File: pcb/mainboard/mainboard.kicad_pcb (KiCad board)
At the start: 10 copper layers, 585 parts, among them J1 CONN_PCIE_PWR_8PIN, J10 FAN_01, J11 XILINX_JTAG, J12 JUMPER_0402_SPDT, J13 JUMPER_0402_SPDT, J14 RJ45, J15 PMOD_HOST, J16 SMPM, J17 SMPM, J18 SMPM, J19 SMPM, J2 CONN_IBC_MGMT, J20 SMPM, J21 SMPM, J22 SMPM, J23 SMPM, J24 SMPM, J25 SMPM, J26 SMPM, J27 0826-1G1T-23-F, J28 SMPM, J29 SMPM, J3 CONN_01X03, J30 SMPM, J31 SMPM, J32 SMPM, J33 SMPM, J34 SMPM, J35 SMPM, J36 SMPM, J37 SMPM, J38 SMPM, J39 SMPM, J4 CONN_01X05, J40 SMPM, J41 SMPM, J42 SMPM, J43 SMPM, J44 SMPM, J45 SMPM, J46 SMPM, J47 SMPM, J48 CONN_01X10, J5 XILINX_JTAG, J6 CONN_SFP_HOST, J7 SFP_CAGE, J8 FAN_01, J9 CONN_01X03, K1 RELAY_TE_HF3_96, K2 RELAY_TE_HF3_96, K3 RELAY_TE_HF3_96, K4 RELAY_TE_HF3_96, M1 960-23-23-F-AB-0, SW1 SWITCH, SW2 SWITCH, U1 STM32L031C6U6, U10 MAX40026, U11 MAX40026, U12 MAX40026, U13 MAX40026, U14 MAX40026, U15 MAX40026, U16 MAX40026, U17 MAX40026, U18 MAX40026, U19 MAX40026, U2 MYMGK1R812ERSR, U20 MAX40026, U21 DAC60508, U22 DAC60508, U23 STM32H735-UFBGA176-25, U24 AT24MAC402, U25 ADM3101E_QFN, U26 LMR70503, U27 SIT9121AI-2BF-XXS200.000000G, U28 SIT9121AI-2BF-XXS156.250000G, U29 HMC675LP3E, U3 MYMGK00504ERSR, U30 SIT9121AI-2BF-XXS200.000000G, U31 ECS-1612MV-250-CN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

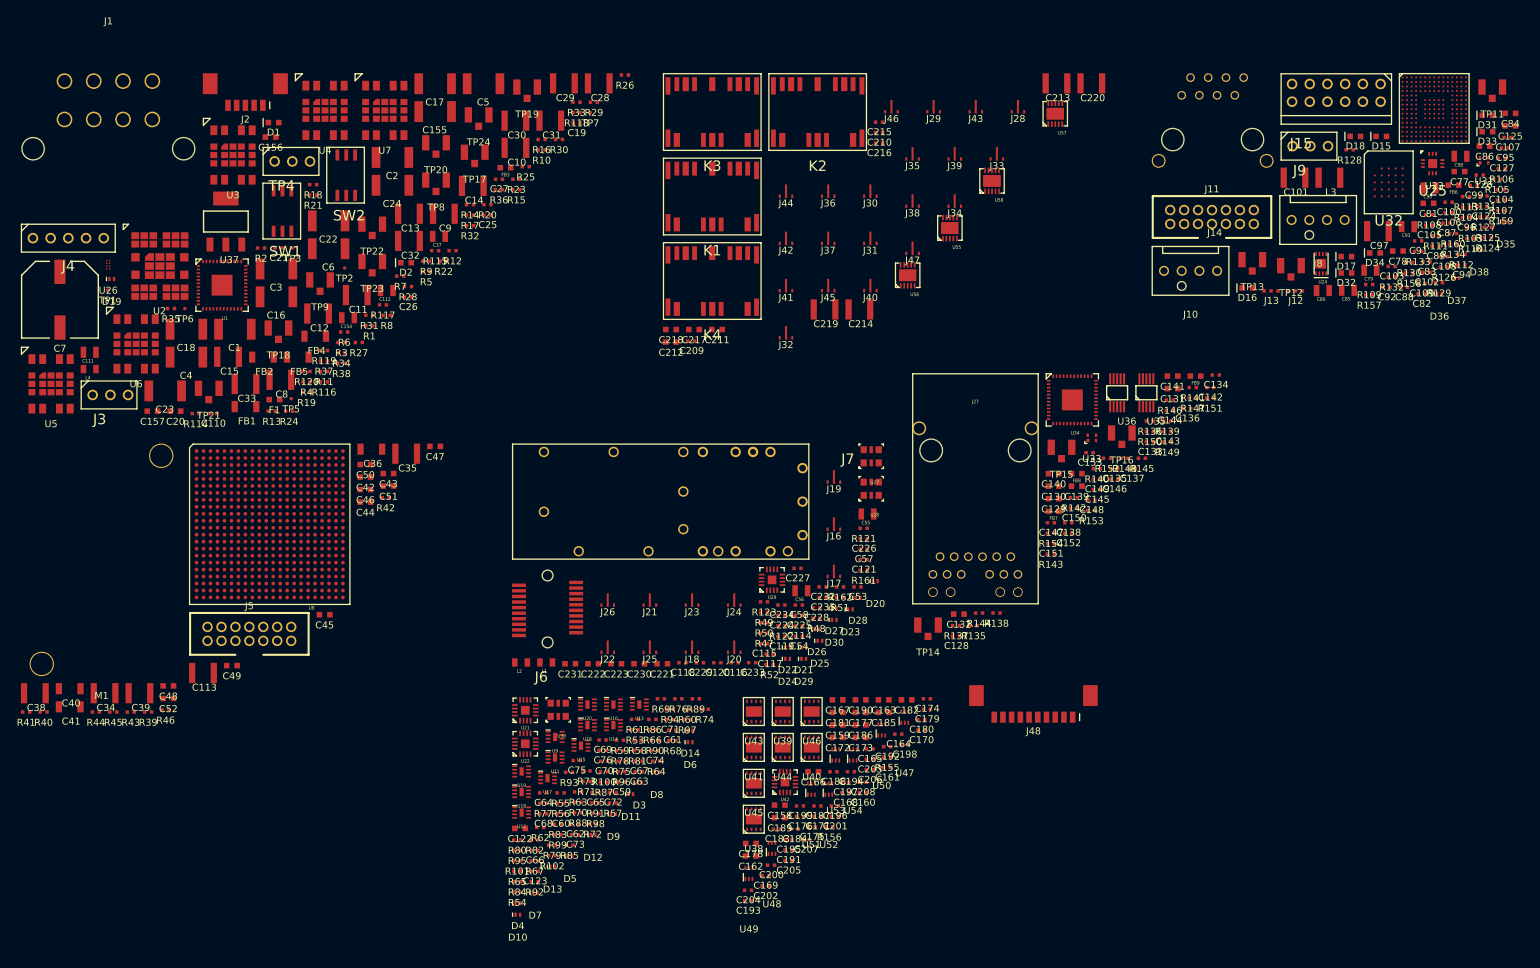
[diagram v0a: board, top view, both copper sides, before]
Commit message: Finished initial schematic review of trigger crossbar mainboard
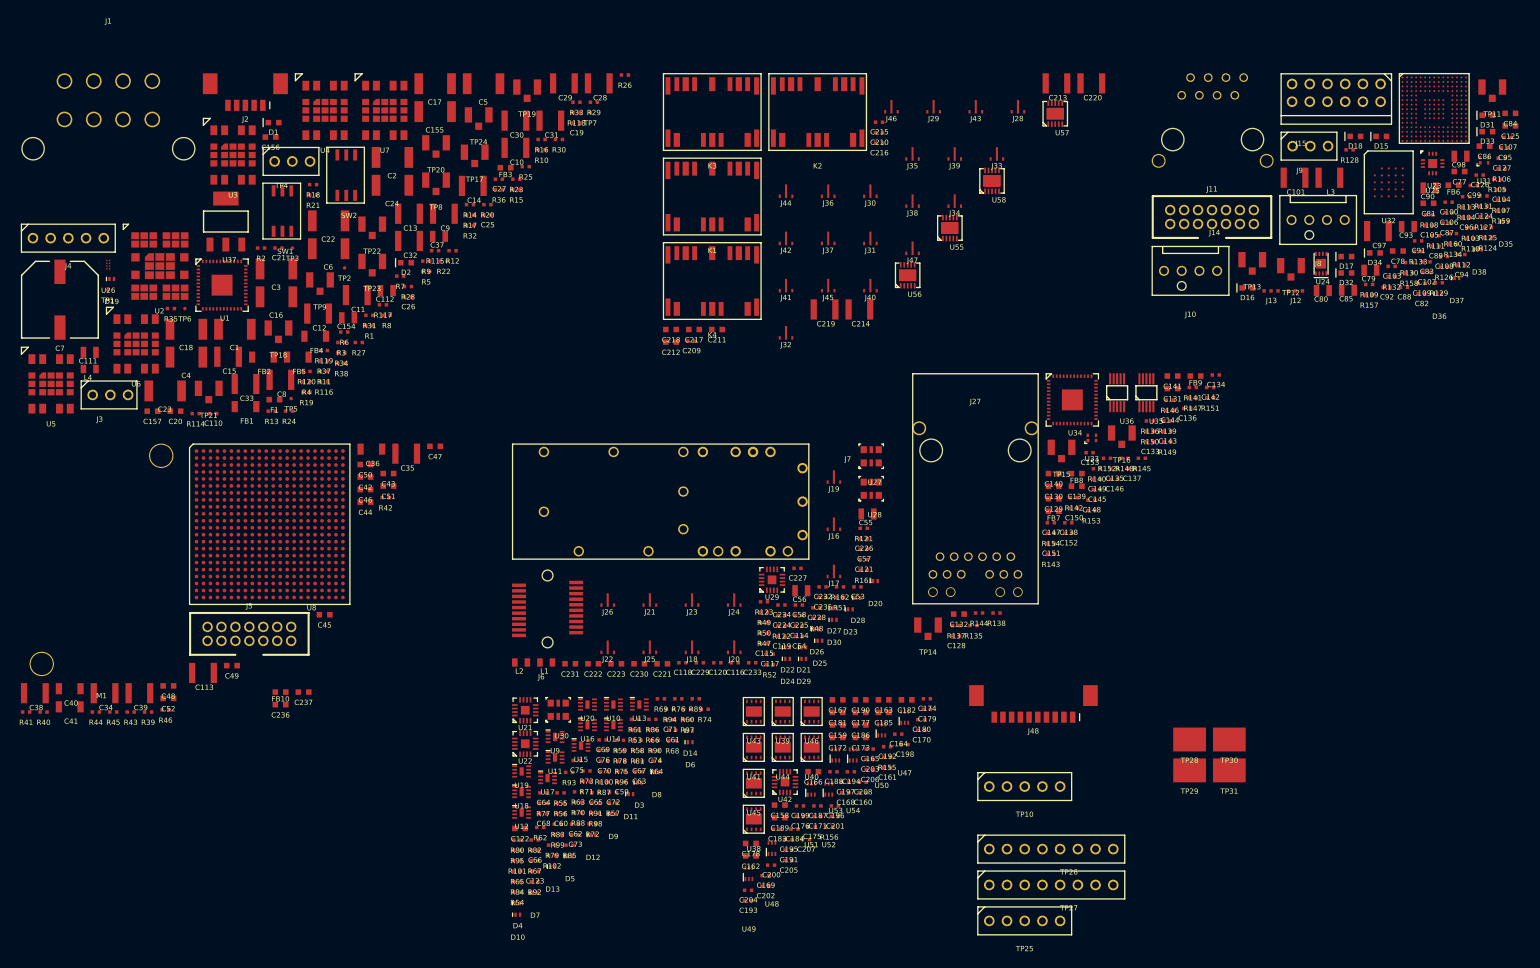
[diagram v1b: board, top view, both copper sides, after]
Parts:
- added C236: 4.7 uF, azonenberg_pcb:EIA_0603_CAP_NOSILK, F.Cu at (63.0, 118.8)
- added C237: 4.7 uF, azonenberg_pcb:EIA_0603_CAP_NOSILK, F.Cu at (66.2, 117.0)
- added FB10: MI0603J601R-10, azonenberg_pcb:EIA_0603_INDUCTOR_NOSILK, F.Cu at (63.0, 117.0)
- added TP10: CONN_01X05, azonenberg_pcb:CONN_HEADER_2.54MM_1x5, F.Cu at (169.7, 130.5)
- added TP25: CONN_01X05, azonenberg_pcb:CONN_HEADER_2.54MM_1x5, F.Cu at (169.7, 149.8)
- added TP26: CONN_01X08, azonenberg_pcb:CONN_HEADER_2.54MM_1x8, F.Cu at (173.5, 139.5)
- added TP27: CONN_01X08, azonenberg_pcb:CONN_HEADER_2.54MM_1x8, F.Cu at (173.5, 144.6)
- added TP28: TESTCLIP, azonenberg_pcb:TESTPOINT_SMT_KEYSTONE_5016, F.Cu at (193.3, 123.8)
- added TP29: TESTCLIP, azonenberg_pcb:TESTPOINT_SMT_KEYSTONE_5016, F.Cu at (193.3, 128.2)
- added TP30: TESTCLIP, azonenberg_pcb:TESTPOINT_SMT_KEYSTONE_5016, F.Cu at (199.1, 123.8)
- added TP31: TESTCLIP, azonenberg_pcb:TESTPOINT_SMT_KEYSTONE_5016, F.Cu at (199.1, 128.2)
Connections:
- net /Inputs/RX_DAC0_CS_N renamed /Management/RX_DAC0_CS_N
- net /Inputs/RX_DAC1_CS_N renamed /Management/RX_DAC1_CS_N
- net Net-(C116-Pad1) renamed /Transceivers/GTC1_P
- net Net-(C117-Pad1) renamed /Transceivers/GTC1_N
- net Net-(C118-Pad1) renamed /Transceivers/GTC2_P
- net Net-(C119-Pad1) renamed /Transceivers/GTC2_N
- C132 pad 1: /1V2 -> /1000base-T PHY/D1V2
- C138 pad 1: /1V2 -> /1000base-T PHY/D1V2
- C143 pad 1: /1V2 -> /1000base-T PHY/D1V2
- C147 pad 1: /1V2 -> /1000base-T PHY/D1V2
- C150 pad 1: /1V2 -> /1000base-T PHY/D1V2
- C152 pad 1: /1V2 -> /1000base-T PHY/D1V2
- C153 pad 1: /1V2 -> /1000base-T PHY/D1V2
- C174 pad 1: /1V8 -> /3V3
- C75 pad 1: /1V8 -> /3V3
- C76 pad 1: /1V8 -> /3V3
- J48 pad 3: /Management/SOFT_POWER -> /SOFT_POWER
- J48 pad 8: /Management/SOFT_RESET -> /SOFT_RESET
- U21 pad 16: /1V8 -> /3V3
- U22 pad 16: /1V8 -> /3V3
- U34 pad 14: /1V2 -> /1000base-T PHY/D1V2
- U34 pad 18: /1V2 -> /1000base-T PHY/D1V2
- U34 pad 23: /1V2 -> /1000base-T PHY/D1V2
- U34 pad 26: /1V2 -> /1000base-T PHY/D1V2
- U34 pad 30: /1V2 -> /1000base-T PHY/D1V2
- U34 pad 39: /1V2 -> /1000base-T PHY/D1V2
- U42 pad 16: /1V8 -> /3V3

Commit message: Initial floorplanning work, added SFP+ LEDs
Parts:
- added D39: GREEN, azonenberg_pcb:EIA_0603_LED, F.Cu at (279.8, 55.5)
- added D40: GREEN, azonenberg_pcb:EIA_0603_LED, F.Cu at (283.5, 55.5)
- added MH1: SCREWHOLE, azonenberg_pcb:MECHANICAL_CLEARANCEHOLE_4_40, F.Cu at (143.0, 135.0)
- added MH2: SCREWHOLE, azonenberg_pcb:MECHANICAL_CLEARANCEHOLE_4_40, F.Cu at (143.0, 24.0)
- added MH3: SCREWHOLE, azonenberg_pcb:MECHANICAL_CLEARANCEHOLE_4_40, F.Cu at (199.0, 24.0)
- added MH4: SCREWHOLE, azonenberg_pcb:MECHANICAL_CLEARANCEHOLE_4_40, F.Cu at (275.0, 25.0)
- added MH5: SCREWHOLE, azonenberg_pcb:MECHANICAL_CLEARANCEHOLE_4_40, F.Cu at (269.0, 135.0)
- added MH6: SCREWHOLE, azonenberg_pcb:MECHANICAL_CLEARANCEHOLE_4_40, F.Cu at (224.0, 135.0)
- added R163: 470, azonenberg_pcb:EIA_0402_RES_NOSILK, F.Cu at (278.9, 57.4)
- added R164: 470, azonenberg_pcb:EIA_0402_RES_NOSILK, F.Cu at (281.4, 57.4)
- moved C222 228.2 mm to (336.0, 117.5)
- moved C231 218.6 mm to (323.0, 118.2)
- moved C102 204.7 mm to (75.5, 194.0)
- moved C103 204.7 mm to (70.5, 193.2)
- moved C105 204.7 mm to (75.9, 187.3)
- moved C107 204.7 mm to (87.1, 174.7)
- moved C108 204.7 mm to (78.0, 191.8)
- moved C109 204.7 mm to (74.8, 195.6)
- moved C125 204.7 mm to (87.5, 173.0)
- moved C126 204.7 mm to (83.1, 180.1)
- moved C127 204.7 mm to (86.3, 177.7)
- moved C78 204.7 mm to (71.4, 191.0)
- moved C81 204.7 mm to (75.8, 184.1)
- moved C82 204.7 mm to (74.8, 197.1)
- moved C83 204.7 mm to (75.5, 192.5)
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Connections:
- U8 pad L19: unconnected-(U8-PadL19) -> /Management/SFP_LED1
- U8 pad L20: unconnected-(U8-PadL20) -> /Management/SFP_LED2
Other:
- board outline added: 145 x 121 mm
- rule pad_to_mask_clearance: 0 -> 0.05
- board text added: "BERT ports"
- board text added: "CDR input"
- board text added: "GTX clocks"
- board text added: "OUTPUTS"
- board text added: "Output level"

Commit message: Continued initial layout work
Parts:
- C133, C134, C135, C136, C137, C138, C142, C143, C144, C145, C146, C147, C148, C149, C150, C151, C152, C153, C53, C54, C55, C56, C57, C58, L1, L2, R135, R136, R138, R146, R148, R149, R150, R151, R152, R153, R161, R162, R163, R164, R48, R49, R50, R51, R52: moved to B.Cu
- moved R132 391.6 mm to (450.2, 99.1)
- moved R128 390.0 mm to (446.7, 99.0)
- moved D32 388.8 mm to (432.4, 69.8)
- moved R133 386.3 mm to (450.2, 102.2)
- moved R157 383.8 mm to (428.1, 66.5)
- moved D34 381.5 mm to (431.9, 76.5)
- moved R129 381.0 mm to (446.6, 102.0)
- moved R130 380.0 mm to (442.9, 105.6)
- moved R126 377.1 mm to (443.1, 99.2)
- moved R158 376.5 mm to (428.4, 69.8)
- moved D16 376.0 mm to (403.7, 69.5)
- moved J13 374.0 mm to (390.4, 35.0)
- moved J12 371.9 mm to (390.3, 32.4)
- moved R131 371.4 mm to (446.8, 105.2)
- moved R134 369.7 mm to (439.4, 106.1)
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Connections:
- R148 pad 1: /1000base-T PHY/1V8_IO -> /3V3
- R149 pad 1: /1000base-T PHY/1V8_IO -> /3V3
- R150 pad 1: /1000base-T PHY/1V8_IO -> /3V3
- R154 pad 1: /1000base-T PHY/1V8_IO -> /3V3
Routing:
- net /GND: track 0.00 -> 241.8 mm, vias 0 -> 48
- net /3V3: track 0.00 -> 69.1 mm, vias 0 -> 15
- net /1000base-T PHY/ETH_B_P: track 0.00 -> 20.9 mm
- net /1000base-T PHY/ETH_B_N: track 0.00 -> 20.9 mm
- net /1000base-T PHY/ETH_C_N: track 0.00 -> 20.5 mm
- net /1000base-T PHY/ETH_C_P: track 0.00 -> 20.5 mm
- net /1000base-T PHY/ETH_D_N: track 0.00 -> 18.0 mm
- net /1000base-T PHY/ETH_D_P: track 0.00 -> 18.0 mm
- net /1000base-T PHY/ETH_A_P: track 0.00 -> 17.8 mm
- net /1000base-T PHY/ETH_A_N: track 0.00 -> 17.8 mm
- net /1000base-T PHY/A3V3: track 0.00 -> 16.6 mm, vias 0 -> 5
- net /1000base-T PHY/D1V2: track 0.00 -> 16.1 mm, vias 0 -> 6
- net /Management/SFP_TX_FAULT: track 0.00 -> 11.7 mm, vias 0 -> 1
- net /Management/SFP_TX_DISABLE: track 0.00 -> 10.7 mm, vias 0 -> 1
- net /Transceivers/SFP_I2C_SDA: track 0.00 -> 10.7 mm, vias 0 -> 1
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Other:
- board text added: "FPGA LEDs"
- board text added: "FPGA flash"
- board text added: "Fans"
- board text added: "MCU"
- board text added: "MCU LEDs"

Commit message: Initial MCU subsystem layout
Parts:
- added C238: 0.47 uF, azonenberg_pcb:EIA_0402_CAP_NOSILK, B.Cu at (236.6, 62.7)
- added TP32: U.FL, azonenberg_pcb:CONN_U.FL_TE_1909763-1, F.Cu at (248.5, 70.0)
- C100, C102, C103, C104, C105, C124, C77, C78, C80, C82, C83, C85, C86, C87, C88, C89, C91, C92, C95, C96, C99, FB6, R103: moved to B.Cu
- moved D32 241.3 mm to (205.3, 151.5)
- moved R157 241.3 mm to (201.1, 148.3)
- moved R158 241.3 mm to (201.3, 151.5)
- moved D31 241.3 mm to (205.1, 148.6)
- moved D33 241.3 mm to (205.7, 154.9)
- moved D34 241.3 mm to (204.8, 158.2)
- moved R159 241.3 mm to (201.3, 154.8)
- moved R160 241.3 mm to (200.7, 157.9)
- moved U25 179.4 mm to (216.0, 42.0), turned to 90 degrees
- moved J13 176.4 mm to (214.0, 38.2)
- moved C106 173.1 mm to (213.2, 41.8), turned to 90 degrees
- moved J12 172.4 mm to (218.0, 38.2)
- moved C107 169.0 mm to (217.2, 39.5)
- moved C108 168.2 mm to (214.5, 44.5), turned to 180 degrees
- moved C109 164.9 mm to (218.5, 42.0), turned to 90 degrees
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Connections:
- U23 pad B2: unconnected-(U23-PadB2) -> /Management/SFP_RX_LOS
- U23 pad C1: unconnected-(U23-PadC1) -> /Management/SFP_MOD_ABS
- U23 pad D1: unconnected-(U23-PadD1) -> /Management/SFP_TX_FAULT
- U23 pad D2: unconnected-(U23-PadD2) -> /Management/SFP_TX_DISABLE
- U23 pad F15: unconnected-(U23-PadF15) -> /Management/MCU_LED3
- U23 pad G15: unconnected-(U23-PadG15) -> /Management/MCU_LED2
- U23 pad G3: /Management/SFP_TX_FAULT -> unconnected-(U23-PadG3)
- U23 pad H15: unconnected-(U23-PadH15) -> /Management/MCU_LED1
- U23 pad H2: /Management/SFP_TX_DISABLE -> unconnected-(U23-PadH2)
- U23 pad H3: /Management/SFP_RX_LOS -> unconnected-(U23-PadH3)
- U23 pad H4: /Management/SFP_MOD_ABS -> unconnected-(U23-PadH4)
- U23 pad J15: unconnected-(U23-PadJ15) -> /Management/MCU_LED0
- U23 pad N10: /Management/MCU_LED3 -> unconnected-(U23-PadN10)
- U23 pad N11: /Management/MCU_LED1 -> unconnected-(U23-PadN11)
- U23 pad P11: /Management/MCU_LED0 -> unconnected-(U23-PadP11)
- U23 pad R10: /Management/MCU_LED2 -> unconnected-(U23-PadR10)
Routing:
- net /GND: track 241.8 -> 505.2 mm, vias 48 -> 149
- net /3V3: track 69.1 -> 188.2 mm, vias 15 -> 45
- net /Management/VSMPS: track 0.00 -> 44.4 mm, vias 0 -> 15
- net /Management/SFP_RX_LOS: track 6.99 -> 47.0 mm, vias 1 -> 2
- net /Transceivers/SFP_TX_N: track 3.83 -> 40.4 mm
- net /Transceivers/SFP_TX_P: track 3.83 -> 40.2 mm
- net /Management/SFP_MOD_ABS: track 8.61 -> 44.5 mm, vias 1 -> 2
- net /Transceivers/SFP_RX_P: track 3.73 -> 34.1 mm
- net /Transceivers/SFP_RX_N: track 3.73 -> 34.1 mm
- net /Management/SFP_TX_DISABLE: track 10.7 -> 39.6 mm, vias 1 -> 2
- net /Management/VCORE: track 0.00 -> 26.8 mm, vias 0 -> 4
- net /Management/SFP_TX_FAULT: track 11.7 -> 37.1 mm, vias 1 -> 2
- net /Management/MCU_JTAG_TMS: track 0.00 -> 21.0 mm, vias 0 -> 1
- net /1000base-T PHY/ETH_LED2_N: track 1.15 -> 21.7 mm, vias 0 -> 1
- net /Transceivers/SFP_I2C_SCL: track 9.54 -> 28.3 mm, vias 1 -> 2
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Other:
- board text added: "A1V2"
- board text added: "A1V2_ PLL"
- board text added: "A3V3"
- board text added: "BL"
- board text added: "BOOT0"
- board text added: "D1V2"
- board text added: "Fast sync"
- board text added: "INPUTS"
- board text added: "LED0"
- board text added: "LED1"
- board text added: "LED2"
- board text added: "LED3"
- board text added: "MCU JTAG"
- board text added: "NORM"
- board text added: "VCORE"
- board text added: "VSMPS"
- board text removed: "MCU"
- board text removed: "MCU LEDs"

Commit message: Initial placement of rear I/O connectors
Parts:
- C236, C237, FB10: moved to B.Cu
- moved C111 226.1 mm to (260.9, 115.1)
- moved L4 225.7 mm to (260.9, 111.8)
- moved R106 225.2 mm to (91.8, 38.4)
- moved C101 225.2 mm to (110.2, 39.2)
- moved D38 225.2 mm to (98.4, 43.1)
- moved R105 225.2 mm to (85.1, 38.4)
- moved C97 225.2 mm to (98.0, 39.0)
- moved D35 225.2 mm to (87.0, 42.5)
- moved D36 225.2 mm to (91.1, 42.4)
- moved D37 225.2 mm to (95.0, 42.6)
- moved U26 224.3 mm to (261.0, 110.0)
- moved D19 223.0 mm to (260.1, 113.5), turned to -90 degrees
- moved TP24 212.1 mm to (268.2, 115.0)
- moved C236 210.6 mm to (249.0, 62.2), turned to 90 degrees
- moved C110 208.4 mm to (261.6, 113.8), turned to 180 degrees
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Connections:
- J24 pad 1: /Transceivers/CDRTRIG_IN -> (no net)
- J24 pad 2: /GND -> (no net)
- TP26 pad 3: /Management/MCU_QSPI_SCK -> /Management/MCU_QSPI_DQ1
- TP26 pad 4: /Management/MCU_QSPI_DQ0 -> /Management/MCU_QSPI_SCK
- TP26 pad 5: /Management/MCU_QSPI_DQ1 -> /Management/MCU_QSPI_DQ3
- TP26 pad 6: /Management/MCU_QSPI_DQ2 -> /Management/MCU_QSPI_DQ0
- TP26 pad 7: /Management/MCU_QSPI_DQ3 -> /Management/MCU_QSPI_DQ2
- U23 pad B4: /TX_DAC_CS_N -> unconnected-(U23-PadB4)
- U23 pad P1: /Management/MCU_IRQ -> unconnected-(U23-PadP1)
- U23 pad P15: unconnected-(U23-PadP15) -> /Management/MCU_IRQ
- U23 pad R9: unconnected-(U23-PadR9) -> /TX_DAC_CS_N
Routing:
- net /GND: track 505.2 -> 754.8 mm, vias 149 -> 426
- net /1V2: track 0.00 -> 136.4 mm, vias 0 -> 11
- net /3V3: track 188.2 -> 290.5 mm, vias 45 -> 65
- net /Management/FAN2_PWM: track 0.00 -> 38.2 mm, vias 0 -> 1
- net /Management/FAN1_PWM: track 0.00 -> 33.4 mm, vias 0 -> 1
- net /3V0_N: track 0.00 -> 32.9 mm, vias 0 -> 18
- net /Management/MCU_UART_TX: track 0.00 -> 26.5 mm, vias 0 -> 1
- net /Management/MCU_UART_RX: track 0.00 -> 25.6 mm, vias 0 -> 1
- net /Transceivers/SFP_I2C_SCL: track 28.3 -> 53.3 mm, vias 2 -> 3
- net /Management/MCU_VDDA: track 4.49 -> 27.9 mm, vias 2 -> 3
- net /3V3_SB: track 0.00 -> 22.2 mm
- net /Management/SFP_RX_LOS: track 47.0 -> 68.6 mm
- net /Transceivers/SFP_I2C_SDA: track 26.9 -> 47.9 mm, vias 2 -> 3
- net /Management/RX_DAC0_CS_N: track 0.00 -> 18.9 mm, vias 0 -> 1
- net /Management/RX_DAC1_CS_N: track 0.00 -> 18.0 mm, vias 0 -> 1
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- added copper zone on F.Cu, net /GND
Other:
- board size 145 x 121 mm -> 165 x 121 mm
- board text added: "3V0_N"
- board text added: "CDR TRIG"
- board text added: "CS#"
- board text added: "DQ0"
- board text added: "DQ1"
- board text added: "DQ2"
- board text added: "DQ3"
- board text added: "GND"
- board text added: "IN0"
- board text added: "IN1"
- board text added: "IN2"
- board text added: "IN3"
- board text added: "IN4"
- board text added: "IN5"
- board text added: "IN6"
- board text added: "IN7"
- board text added: "IO10"
- board text added: "IO11"
- board text added: "IO8"
- board text added: "IO9"
- board text added: "IRQ"
- board text added: "OUT0"
- board text added: "OUT1"
- board text added: "OUT2"
- board text added: "OUT3"
- board text added: "OUT4"
- board text added: "OUT5"
- board text added: "OUT6"
- board text added: "OUT7"
- board text added: "RX0_N"
- board text added: "RX0_P"
- board text added: "RX1_N"
- board text added: "RX1_P"
- board text added: "SCK"
- board text added: "SYNC_N"
- board text added: "SYNC_P"
- board text added: "TX0_N"
- board text added: "TX0_P"
- board text added: "TX1_N"
- board text added: "TX1_P"
- board text added: "VDDA"
- board text removed: "BERT ports"
- board text removed: "CDR input"
- board text removed: "Fans"
- board text removed: "Fast sync"
- board text removed: "OUTPUTS"
